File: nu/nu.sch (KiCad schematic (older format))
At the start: 11 parts

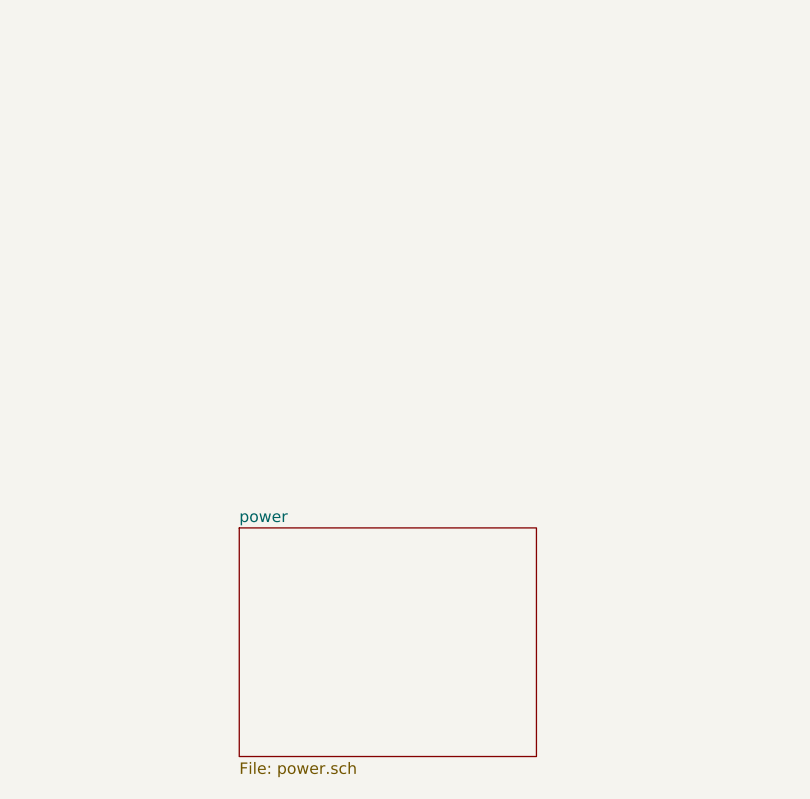
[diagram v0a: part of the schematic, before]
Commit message: Added block diagram, and added some components to the schematic that will end up being removed :/
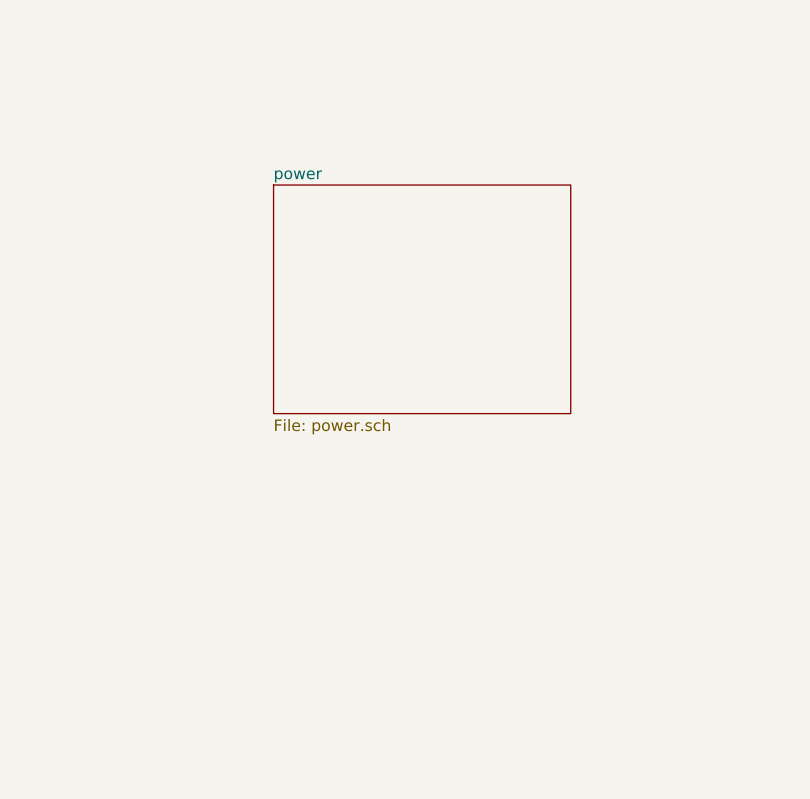
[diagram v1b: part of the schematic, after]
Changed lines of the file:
@@
 $EndDescr
 $Sheet
-S 4200 3700 1300 1000
+S 4350 2200 1300 1000
 U 5C100B31
 F0 "power" 50

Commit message: Updated block diagram
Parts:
- J? (x8): symbol custom:PTH_1_mm -> nu-rescue:PTH_1_mm-custom
- J? (x2): symbol custom:PTH_3_mm -> nu-rescue:PTH_3_mm-custom
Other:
- note added: "XT60 MALE CABLE ASSEMBLY\nADD 4 mm STRAIN RELIEF HOLES"
- note removed: "ADD 4 mm STRAIN RELIEF HOLES"
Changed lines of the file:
@@
 $EndComp
 $Comp
-L custom:PTH_3_mm J?
+L nu-rescue:PTH_3_mm-custom J?
 U 1 1 5C162A1D
 P 1250 4200
@@
 $EndComp
 $Comp
-L custom:PTH_3_mm J?
+L nu-rescue:PTH_3_mm-custom J?
 U 1 1 5C162B98
 P 1250 3950
@@
 Text Notes 9500 1000 2    67   ~ 0
 INDICATE POS AND NEG\nON SILKSCREEN
-Text Notes 750  4500 0    67   ~ 0
-ADD 4 mm STRAIN RELIEF HOLES
+Text Notes 800  4600 0    67   ~ 0
+XT60 MALE CABLE ASSEMBLY\nADD 4 mm STRAIN RELIEF HOLES
 Wire Wire Line
 	8950 1250 8200 1250
@@
 	9950 2700 10100 2700
 $Comp
-L custom:PTH_1_mm J?
+L nu-rescue:PTH_1_mm-custom J?
 U 1 1 5C14202A
 P 10550 2200
@@
 $EndComp
 $Comp
-L custom:PTH_1_mm J?
+L nu-rescue:PTH_1_mm-custom J?
 U 1 1 5C1420FB
 P 10550 2400
@@
 $EndComp
 $Comp
-L custom:PTH_1_mm J?
+L nu-rescue:PTH_1_mm-custom J?
 U 1 1 5C142269
 P 10550 2700
@@
 $EndComp
 $Comp
-L custom:PTH_1_mm J?
+L nu-rescue:PTH_1_mm-custom J?
 U 1 1 5C14226F
 P 10550 2900
@@
 $EndComp
 $Comp
-L custom:PTH_1_mm J?
+L nu-rescue:PTH_1_mm-custom J?
 U 1 1 5C1426F8
 P 10550 3200
@@
 $EndComp
 $Comp
-L custom:PTH_1_mm J?
+L nu-rescue:PTH_1_mm-custom J?
 U 1 1 5C1426FE
 P 10550 3400
@@
 $EndComp
 $Comp
-L custom:PTH_1_mm J?
+L nu-rescue:PTH_1_mm-custom J?
 U 1 1 5C142704
 P 10550 3700
@@
 $EndComp
 $Comp
-L custom:PTH_1_mm J?
+L nu-rescue:PTH_1_mm-custom J?
 U 1 1 5C14270A
 P 10550 3900

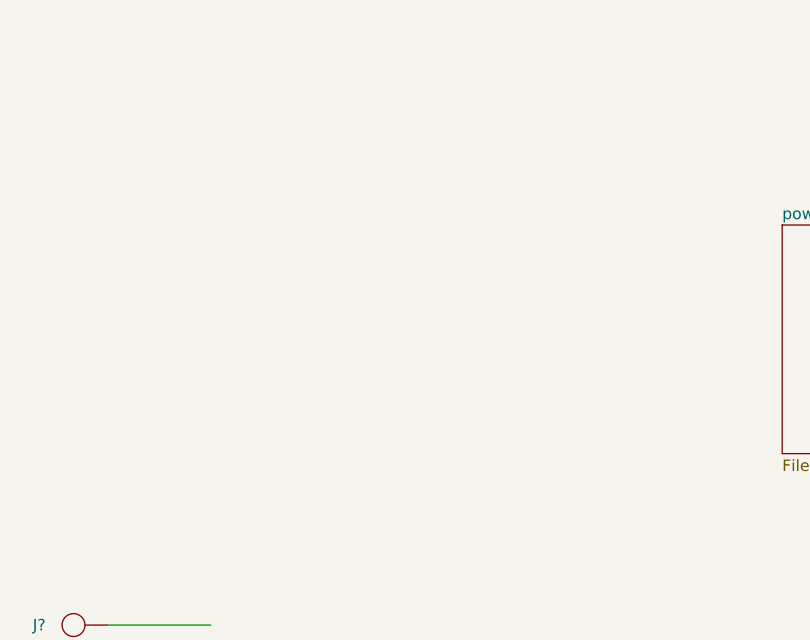
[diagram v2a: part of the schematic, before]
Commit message: added microcontroller sheet
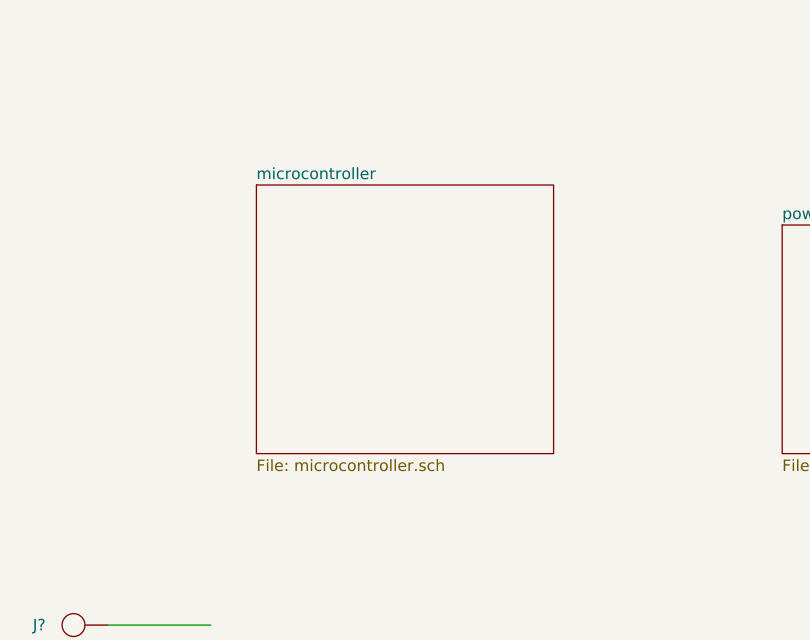
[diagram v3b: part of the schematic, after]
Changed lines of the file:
@@
 $Descr A4 11693 8268
 encoding utf-8
-Sheet 1 3
+Sheet 1 4
 Title ""
 Date ""
@@
 Text Notes 9050 4350 0    67   ~ 0
 ADD 2 mm STRAIN RELIEF HOLES
+$Sheet
+S 2050 2025 1300 1175
+U 5C3EC885
+F0 "microcontroller" 50
+F1 "microcontroller.sch" 50
+$EndSheet
 $EndSCHEMATC
